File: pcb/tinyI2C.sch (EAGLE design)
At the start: 34 parts, among them IC1 74LVC1G125DCK, IC2 74LVC1G125DCK, IC3 IC_LDO_MIC5355, U1 LPC824M201JHI33, X1 TSW-112-02-S-S, X2 TSW-112-02-S-S, X3 TSW-106-02-S-S-RA, X4 TSW-102-02-S-S, X5 TSW-102-02-S-S, X6 TSW-102-02-S-S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

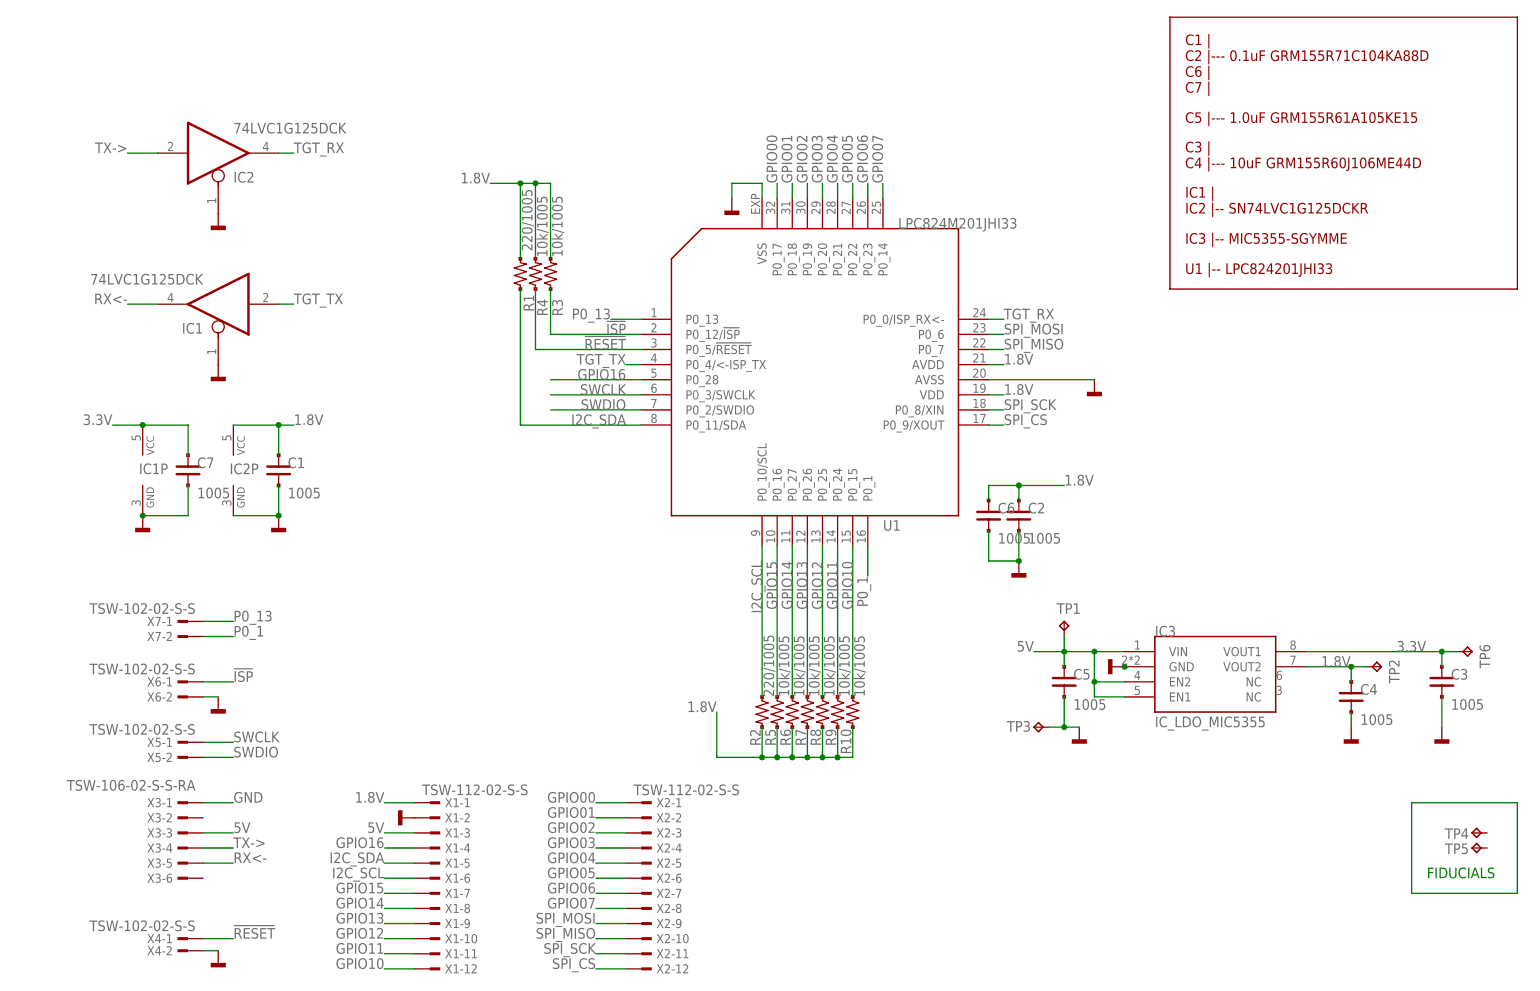
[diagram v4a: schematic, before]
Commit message: [ PCB ][ SCH ] add OSC, capacitors/ replace SPI pins P0_8/P0_9 to be OSC pins added Q1/C8/C9 P0_1 -> SPI CS P0_13 -> SPI SCK
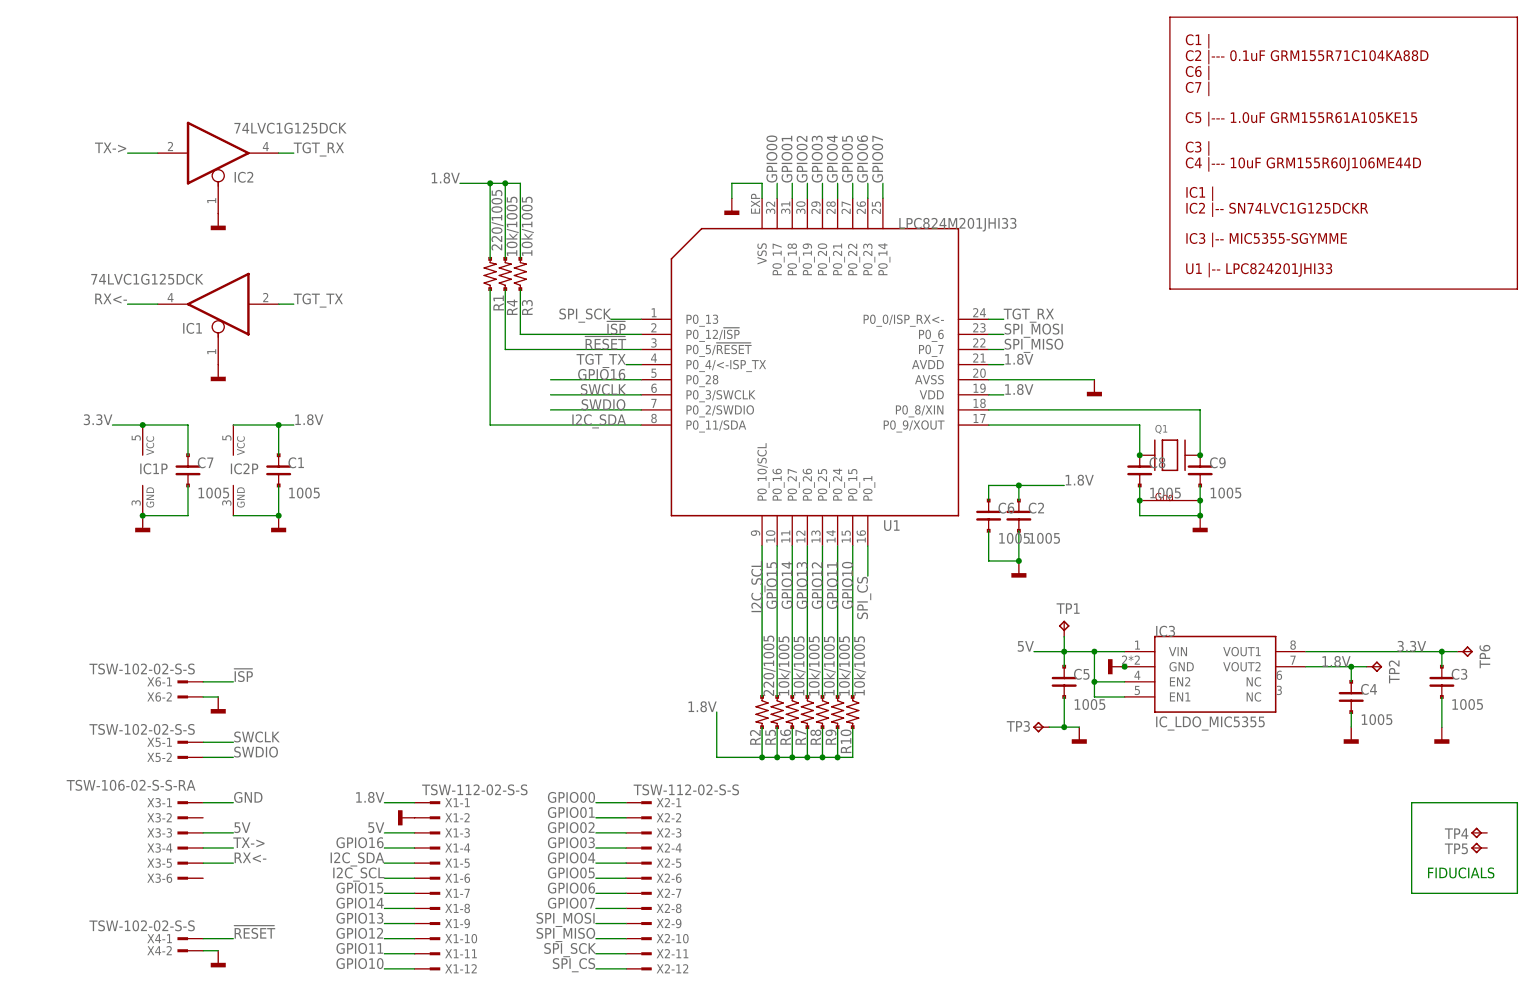
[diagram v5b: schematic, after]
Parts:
- removed X7: TSW-102-02-S-S, con-samtec.local:TSW-102-02-S-S
- added C8, C9: 1005, mylib:C_PAD_PAD_1005
- added Q1: (no value), adafruit (1):XTAL-4-3225
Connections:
- removed net P0_1: U1.P0_1, X7-2.1
- removed net P0_13: U1.P0_13, X7-1.1
- new net N$1: C8.1, Q1.X1, U1.P0_9/XOUT
- new net N$3: C9.1, Q1.X2, U1.P0_8/XIN
- net GND: now also C8.2, C9.2, Q1.G1, Q1.G2
- net SPI_CS: now also U1.P0_1; no longer U1.P0_9/XOUT
- net SPI_SCK: now also U1.P0_13; no longer U1.P0_8/XIN
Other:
- moved on the sheet: R1, R3, R4
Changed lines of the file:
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@@
 <part name="C7" library="mylib" deviceset="C_PAD_PAD_" device="1005" value="1005"/>
 <part name="IC3" library="mylib" deviceset="IC_LDO_MIC5355" device=""/>
-<part name="X7" library="con-samtec.local" deviceset="TSW-102-02-S-S" device=""/>
 <part name="GND3" library="mbed-HDK" deviceset="GND" device=""/>
+<part name="Q1" library="adafruit (1)" deviceset="XTAL-4" device="-3225"/>
+<part name="GND4" library="mbed-HDK" deviceset="GND" device=""/>
+<part name="C8" library="mylib" deviceset="C_PAD_PAD_" device="1005" value="1005"/>
+<part name="C9" library="mylib" deviceset="C_PAD_PAD_" device="1005" value="1005"/>
 </parts>
 <sheets>
@@
 <attribute name="TP_SIGNAL_NAME" x="173.99" y="54.61" size="1.778" layer="97" rot="R90"/>
 </instance>
-<instance part="R1" gate="G$1" x="86.36" y="129.54" smashed="yes" rot="R90">
-<attribute name="NAME" x="88.6714" y="123.19" size="1.778" layer="95" rot="R90"/>
-<attribute name="VALUE" x="88.392" y="133.35" size="1.778" layer="96" rot="R90"/>
+<instance part="R1" gate="G$1" x="81.28" y="129.54" smashed="yes" rot="R90">
+<attribute name="NAME" x="83.5914" y="123.19" size="1.778" layer="95" rot="R90"/>
+<attribute name="VALUE" x="83.312" y="133.35" size="1.778" layer="96" rot="R90"/>
 </instance>
 <instance part="R2" gate="G$1" x="127" y="55.88" smashed="yes" rot="R270">
@@
 <attribute name="VALUE" x="129.032" y="58.42" size="1.778" layer="96" rot="R90"/>
 </instance>
-<instance part="R3" gate="G$1" x="91.44" y="129.54" smashed="yes" rot="R90">
-<attribute name="NAME" x="93.4974" y="122.428" size="1.778" layer="95" rot="R90"/>
-<attribute name="VALUE" x="93.472" y="132.334" size="1.778" layer="96" rot="R90"/>
-</instance>
-<instance part="R4" gate="G$1" x="88.9" y="129.54" smashed="yes" rot="R90">
-<attribute name="NAME" x="90.9574" y="122.428" size="1.778" layer="95" rot="R90"/>
-<attribute name="VALUE" x="90.932" y="132.334" size="1.778" layer="96" rot="R90"/>
+<instance part="R3" gate="G$1" x="86.36" y="129.54" smashed="yes" rot="R90">
+<attribute name="NAME" x="88.4174" y="122.428" size="1.778" layer="95" rot="R90"/>
+<attribute name="VALUE" x="88.392" y="132.334" size="1.778" layer="96" rot="R90"/>
+</instance>
+<instance part="R4" gate="G$1" x="83.82" y="129.54" smashed="yes" rot="R90">
+<attribute name="NAME" x="85.8774" y="122.428" size="1.778" layer="95" rot="R90"/>
+<attribute name="VALUE" x="85.852" y="132.334" size="1.778" layer="96" rot="R90"/>
 </instance>
 <instance part="R5" gate="G$1" x="129.54" y="55.88" smashed="yes" rot="R270">
@@
 <instance part="C7" gate="G$1" x="30.48" y="96.52"/>
 <instance part="IC3" gate="G$1" x="187.96" y="66.04"/>
-<instance part="X7" gate="-1" x="30.48" y="71.12" rot="MR0"/>
-<instance part="X7" gate="-2" x="30.48" y="68.58" rot="MR0"/>
 <instance part="GND3" gate="1" x="22.86" y="88.9"/>
+<instance part="Q1" gate="G$1" x="195.58" y="99.06"/>
+<instance part="GND4" gate="1" x="200.66" y="88.9"/>
+<instance part="C8" gate="G$1" x="190.5" y="96.52"/>
+<instance part="C9" gate="G$1" x="200.66" y="96.52"/>
 </instances>
 <busses>
@@
 <junction x="187.96" y="63.5"/>
 <pinref part="IC3" gate="G$1" pin="GND"/>
+</segment>
+<segment>
+<pinref part="Q1" gate="G$1" pin="G2"/>
+<pinref part="GND4" gate="1" pin="GND"/>
+<wire x1="200.66" y1="88.9" x2="200.66" y2="91.44" width="0.1524" layer="91"/>
+<pinref part="Q1" gate="G$1" pin="G1"/>
+<wire x1="200.66" y1="88.9" x2="190.5" y2="88.9" width="0.1524" layer="91"/>
+<wire x1="190.5" y1="88.9" x2="190.5" y2="91.44" width="0.1524" layer="91"/>
+<junction x="200.66" y="88.9"/>
+<pinref part="C8" gate="G$1" pin="2"/>
+<wire x1="190.5" y1="93.98" x2="190.5" y2="91.44" width="0.1524" layer="91"/>
+<junction x="190.5" y="91.44"/>
+<pinref part="C9" gate="G$1" pin="2"/>
+<wire x1="200.66" y1="91.44" x2="200.66" y2="93.98" width="0.1524" layer="91"/>
+<junction x="200.66" y="91.44"/>
 </segment>
 </net>
@@
 </segment>
 <segment>
-<wire x1="91.44" y1="132.08" x2="91.44" y2="144.78" width="0.1524" layer="91"/>
+<wire x1="86.36" y1="132.08" x2="86.36" y2="144.78" width="0.1524" layer="91"/>
 <pinref part="R3" gate="G$1" pin="2"/>
-<wire x1="88.9" y1="132.08" x2="88.9" y2="144.78" width="0.1524" layer="91"/>
+<wire x1="83.82" y1="132.08" x2="83.82" y2="144.78" width="0.1524" layer="91"/>
 <pinref part="R4" gate="G$1" pin="2"/>
-<wire x1="91.44" y1="144.78" x2="88.9" y2="144.78" width="0.1524" layer="91"/>
+<wire x1="86.36" y1="144.78" x2="83.82" y2="144.78" width="0.1524" layer="91"/>
 <pinref part="R1" gate="G$1" pin="2"/>
-<wire x1="86.36" y1="132.08" x2="86.36" y2="144.78" width="0.1524" layer="91"/>
-<label x="81.28" y="144.78" size="1.778" layer="95" rot="MR0"/>
-<wire x1="88.9" y1="144.78" x2="86.36" y2="144.78" width="0.1524" layer="91"/>
-<junction x="88.9" y="144.78"/>
-<wire x1="86.36" y1="144.78" x2="81.28" y2="144.78" width="0.1524" layer="91"/>
-<junction x="86.36" y="144.78"/>
+<wire x1="81.28" y1="132.08" x2="81.28" y2="144.78" width="0.1524" layer="91"/>
+<label x="76.2" y="144.78" size="1.778" layer="95" rot="MR0"/>
+<wire x1="83.82" y1="144.78" x2="81.28" y2="144.78" width="0.1524" layer="91"/>
+<junction x="83.82" y="144.78"/>
+<wire x1="81.28" y1="144.78" x2="76.2" y2="144.78" width="0.1524" layer="91"/>
+<junction x="81.28" y="144.78"/>
 </segment>
 <segment>
@@
 <label x="104.14" y="119.38" size="1.778" layer="95" rot="MR0"/>
 <pinref part="R3" gate="G$1" pin="1"/>
-<wire x1="91.44" y1="119.38" x2="106.68" y2="119.38" width="0.1524" layer="91"/>
-<wire x1="91.44" y1="127" x2="91.44" y2="119.38" width="0.1524" layer="91"/>
+<wire x1="86.36" y1="119.38" x2="106.68" y2="119.38" width="0.1524" layer="91"/>
+<wire x1="86.36" y1="127" x2="86.36" y2="119.38" width="0.1524" layer="91"/>
 </segment>
 <segment>
@@
 <segment>
 <pinref part="U1" gate="G$1" pin="P0_5/!RESET!"/>
-<wire x1="106.68" y1="116.84" x2="88.9" y2="116.84" width="0.1524" layer="91"/>
-<wire x1="88.9" y1="116.84" x2="88.9" y2="127" width="0.1524" layer="91"/>
+<wire x1="106.68" y1="116.84" x2="83.82" y2="116.84" width="0.1524" layer="91"/>
+<wire x1="83.82" y1="116.84" x2="83.82" y2="127" width="0.1524" layer="91"/>
 <label x="104.14" y="116.84" size="1.778" layer="95" rot="MR0"/>
 <pinref part="R4" gate="G$1" pin="1"/>
@@
 <label x="104.14" y="104.14" size="1.778" layer="95" rot="MR0"/>
 <pinref part="R1" gate="G$1" pin="1"/>
-<wire x1="86.36" y1="127" x2="86.36" y2="104.14" width="0.1524" layer="91"/>
-<wire x1="86.36" y1="104.14" x2="106.68" y2="104.14" width="0.1524" layer="91"/>
+<wire x1="81.28" y1="127" x2="81.28" y2="104.14" width="0.1524" layer="91"/>
+<wire x1="81.28" y1="104.14" x2="106.68" y2="104.14" width="0.1524" layer="91"/>
 </segment>
 <segment>
@@
 <net name="SPI_SCK" class="0">
 <segment>
-<pinref part="U1" gate="G$1" pin="P0_8/XIN"/>
-<label x="167.64" y="106.68" size="1.778" layer="95"/>
-<wire x1="165.1" y1="106.68" x2="167.64" y2="106.68" width="0.1524" layer="91"/>
-</segment>
-<segment>
 <wire x1="99.06" y1="15.24" x2="104.14" y2="15.24" width="0.1524" layer="91"/>
 <pinref part="X2" gate="-11" pin="1"/>
 <label x="99.06" y="15.24" size="1.778" layer="95" rot="MR0"/>
 </segment>
+<segment>
+<pinref part="U1" gate="G$1" pin="P0_13"/>
+<wire x1="106.68" y1="121.92" x2="101.6" y2="121.92" width="0.1524" layer="91"/>
+<label x="101.6" y="121.92" size="1.778" layer="95" rot="MR0"/>
+</segment>
 </net>
 <net name="SPI_CS" class="0">
-<segment>
-<pinref part="U1" gate="G$1" pin="P0_9/XOUT"/>
-<label x="167.64" y="104.14" size="1.778" layer="95"/>
-<wire x1="165.1" y1="104.14" x2="167.64" y2="104.14" width="0.1524" layer="91"/>
-</segment>
 <segment>
 <wire x1="99.06" y1="12.7" x2="104.14" y2="12.7" width="0.1524" layer="91"/>
 <pinref part="X2" gate="-12" pin="1"/>
 <label x="99.06" y="12.7" size="1.778" layer="95" rot="MR0"/>
+</segment>
+<segment>
+<pinref part="U1" gate="G$1" pin="P0_1"/>
+<wire x1="144.78" y1="83.82" x2="144.78" y2="78.74" width="0.1524" layer="91"/>
+<label x="144.78" y="78.74" size="1.778" layer="95" rot="MR270"/>
 </segment>
 </net>
@@
 </segment>
 </net>
-<net name="P0_1" class="0">
-<segment>
-<pinref part="U1" gate="G$1" pin="P0_1"/>
-<wire x1="144.78" y1="83.82" x2="144.78" y2="78.74" width="0.1524" layer="91"/>
-<label x="144.78" y="78.74" size="1.778" layer="95" rot="MR270"/>
-</segment>
-<segment>
-<wire x1="33.02" y1="68.58" x2="38.1" y2="68.58" width="0.1524" layer="91"/>
-<label x="38.1" y="68.58" size="1.778" layer="95"/>
-<pinref part="X7" gate="-2" pin="1"/>
-</segment>
-</net>
-<net name="P0_13" class="0">
-<segment>
-<pinref part="U1" gate="G$1" pin="P0_13"/>
-<wire x1="106.68" y1="121.92" x2="101.6" y2="121.92" width="0.1524" layer="91"/>
-<label x="101.6" y="121.92" size="1.778" layer="95" rot="MR0"/>
-</segment>
-<segment>
-<wire x1="38.1" y1="71.12" x2="33.02" y2="71.12" width="0.1524" layer="91"/>
-<pinref part="X7" gate="-1" pin="1"/>
-<label x="38.1" y="71.12" size="1.778" layer="95"/>
-</segment>
-</net>
+<net name="N$1" class="0">
+<segment>
+<pinref part="U1" gate="G$1" pin="P0_9/XOUT"/>
+<pinref part="Q1" gate="G$1" pin="X1"/>
+<wire x1="165.1" y1="104.14" x2="190.5" y2="104.14" width="0.1524" layer="91"/>
+<wire x1="190.5" y1="104.14" x2="190.5" y2="99.06" width="0.1524" layer="91"/>
+<pinref part="C8" gate="G$1" pin="1"/>
+<junction x="190.5" y="99.06"/>
+</segment>
+</net>
+<net name="N$3" class="0">
+<segment>
+<pinref part="U1" gate="G$1" pin="P0_8/XIN"/>
+<pinref part="Q1" gate="G$1" pin="X2"/>
+<wire x1="165.1" y1="106.68" x2="200.66" y2="106.68" width="0.1524" layer="91"/>
+<wire x1="200.66" y1="106.68" x2="200.66" y2="99.06" width="0.1524" layer="91"/>
+<pinref part="C9" gate="G$1" pin="1"/>
+<junction x="200.66" y="99.06"/>
+</segment>
+</net>
